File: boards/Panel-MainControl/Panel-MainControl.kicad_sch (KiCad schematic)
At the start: 16 parts, among them J1 ISP, J2 Raspberry_Pi_2_3, J3 BoardCon, J4 Panel, U1 ATmega48-20P, U2 ICL3232

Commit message: Initial schematics for panel control boards
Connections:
- net +3.3V: now also J2.1 (3V3), J2.17 (3V3)
- no-connect marks 13 -> 14
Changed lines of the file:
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@@
+	)
+	(no_connect
+		(at 146.05 74.93)
 	)
 	(no_connect
@@
 					(unit 1)
 				)
+			)
+		)
+	)
+	(symbol
+		(lib_id "power:+3.3V")
+		(at 156.21 74.93 0)
+		(unit 1)
+		(exclude_from_sim no)
+		(in_bom yes)
+		(on_board yes)
+		(dnp no)
+		(fields_autoplaced yes)
+		(property "Reference" "#PWR022"
+			(at 156.21 78.74 0)
+			(effects
+				(font
+					(size 1.27 1.27)
+				)
+				(hide yes)
+			)
+		)
+		(property "Value" "+3.3V"
+			(at 156.21 69.85 0)
+			(effects
+				(font
+					(size 1.27 1.27)
+				)
+			)
+		)
+		(property "Footprint" ""
+			(at 156.21 74.93 0)
+			(effects
+				(font
+					(size 1.27 1.27)
+				)
+				(hide yes)
+			)
+		)
+		(property "Datasheet" ""
+			(at 156.21 74.93 0)
+			(effects
+				(font
+					(size 1.27 1.27)
+				)
+				(hide yes)
+			)
+		)
+		(property "Description" "Power symbol creates a global label with name \"+3.3V\""
+			(at 156.21 74.93 0)
+			(effects
+				(font
+					(size 1.27 1.27)
+				)
+				(hide yes)
+			)
+		)
+		(pin "1"
+		)
+		(instances
+			(project "Panel-MainControl"
+				(path "/2777062a-260a-49c7-9a79-289c63518b5f"
+					(reference "#PWR022")
+					(unit 1)
+				)

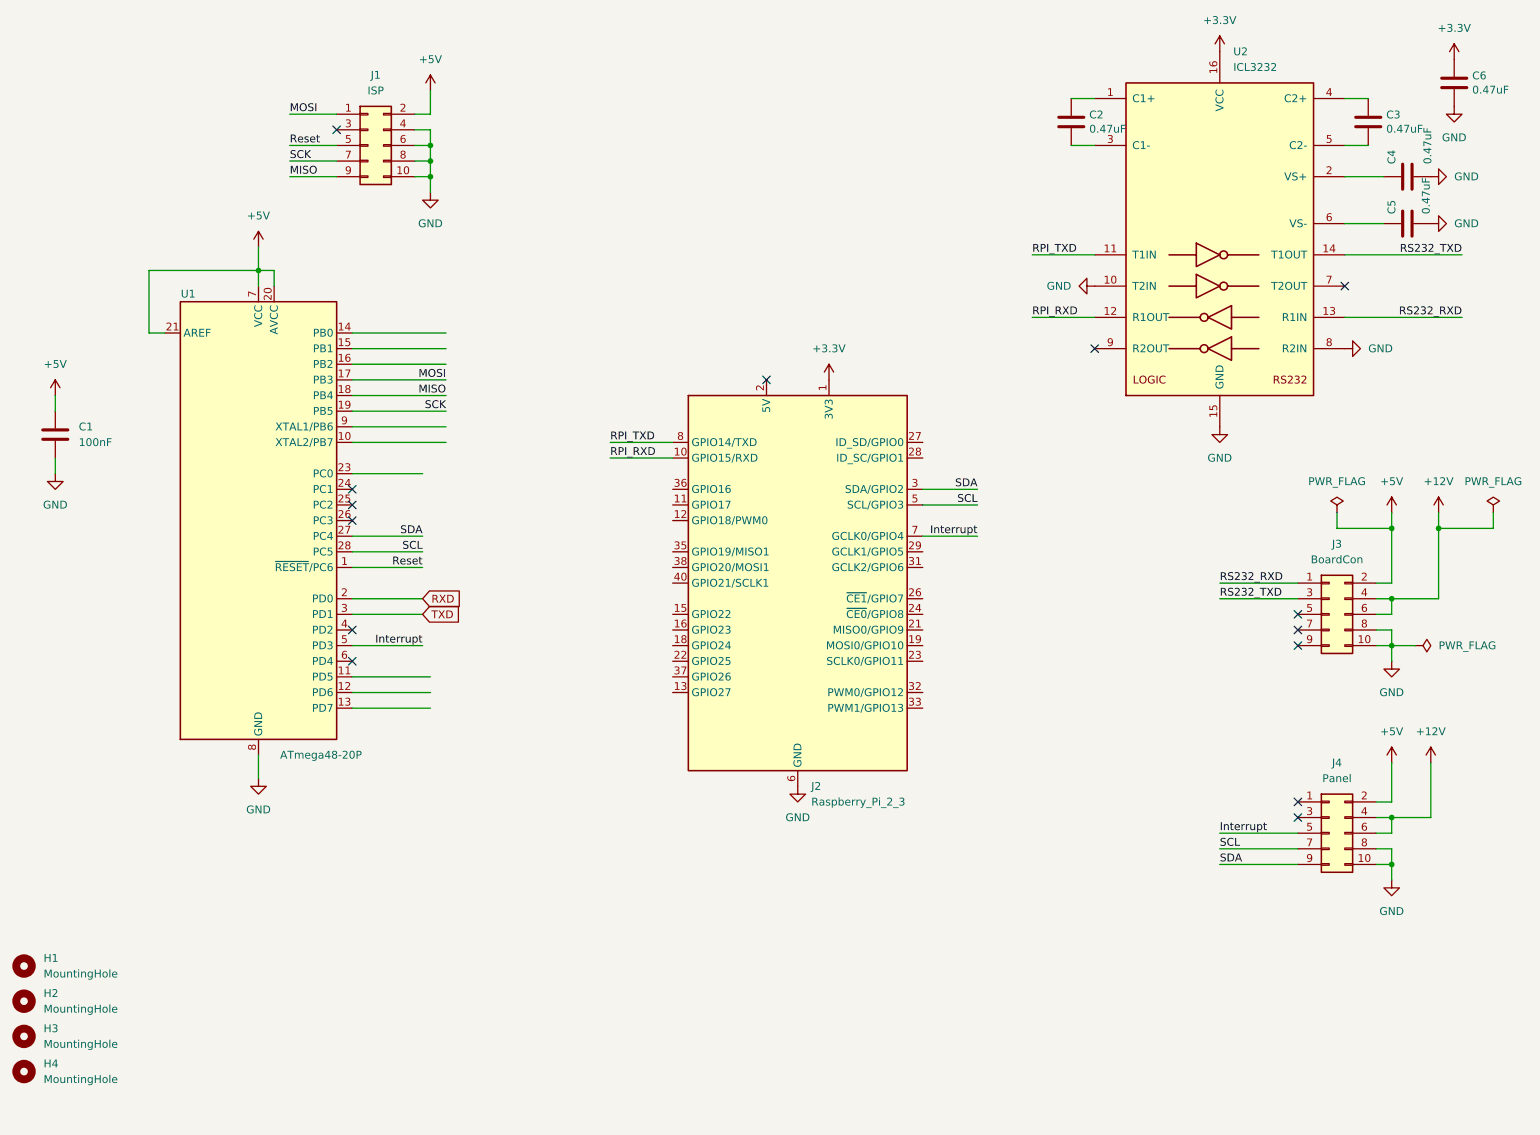
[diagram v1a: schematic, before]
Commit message: Added panel design files and panel schematics
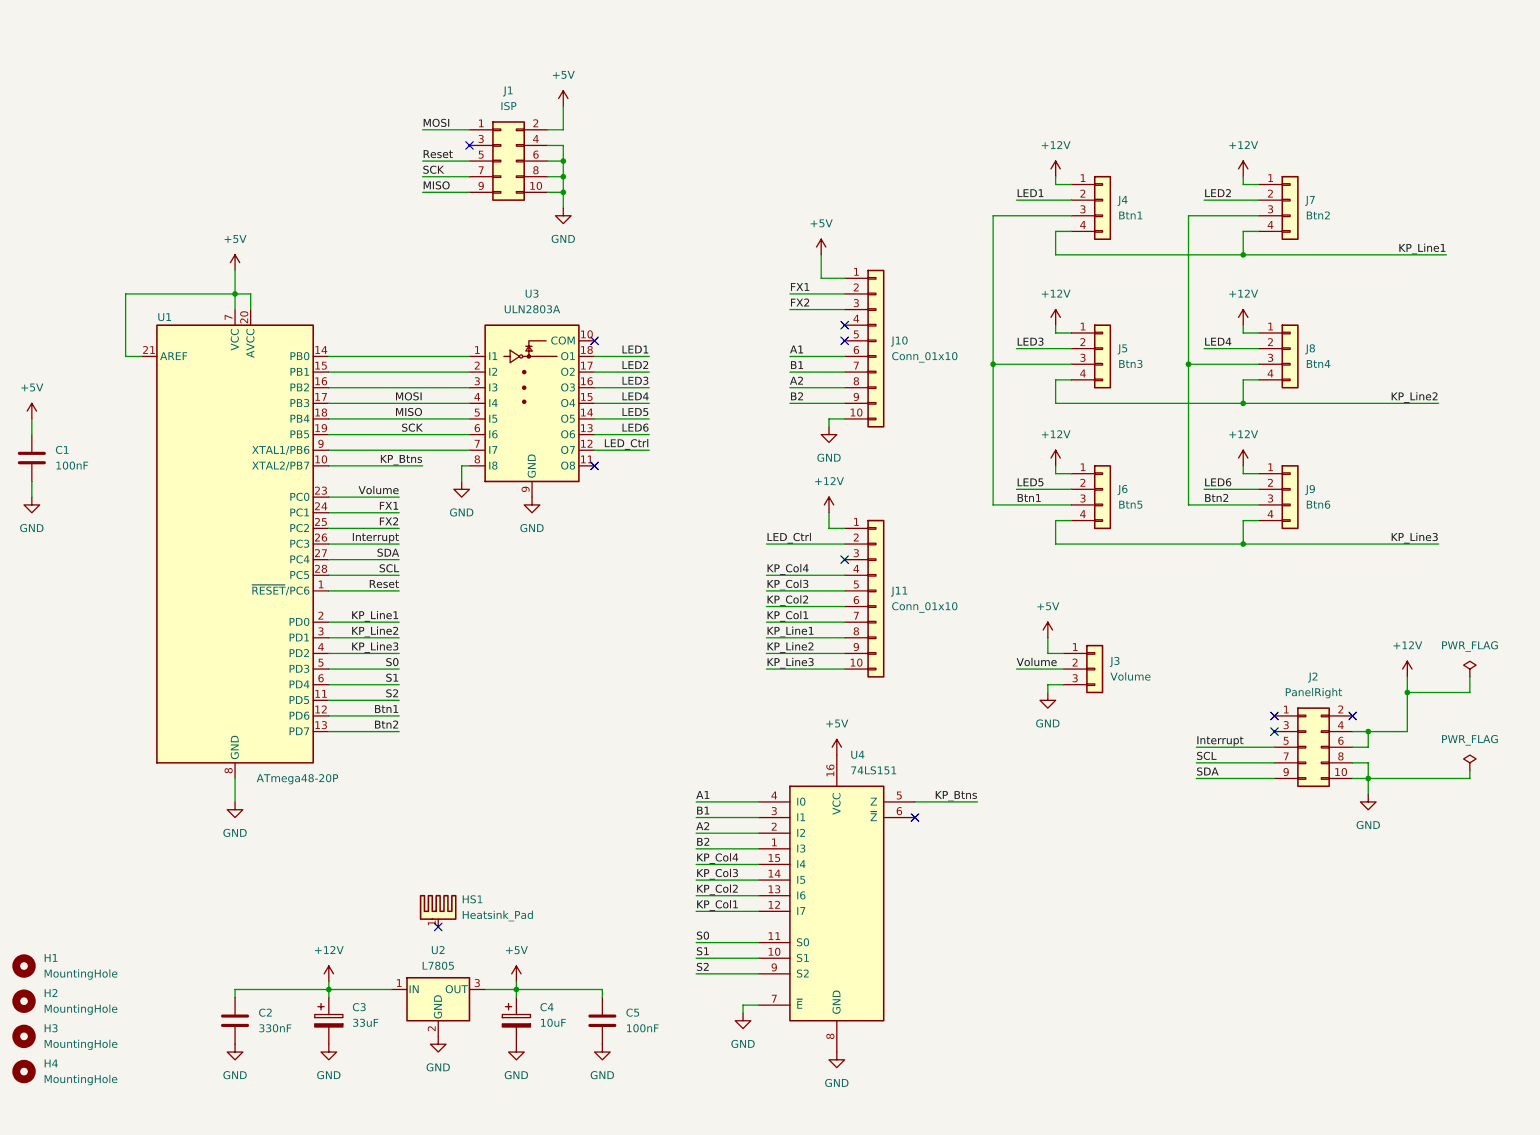
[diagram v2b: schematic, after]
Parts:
- removed C3, C4, C6: 0.47uF, Capacitor_THT:C_Rect_L7.0mm_W3.5mm_P5.00mm, symbol Device:C
- removed J2: Raspberry_Pi_2_3, Connector_PinHeader_2.54mm:PinHeader_2x20_P2.54mm_Vertical, symbol Connector:Raspberry_Pi_2_3
- removed J3: BoardCon, Connector_IDC:IDC-Header_2x05_P2.54mm_Vertical, symbol Connector_Generic:Conn_02x05_Odd_Even
- removed J4: Panel, Connector_IDC:IDC-Header_2x05_P2.54mm_Vertical, symbol Connector_Generic:Conn_02x05_Odd_Even
- removed U2: ICL3232, Package_DIP:DIP-16_W7.62mm, symbol Interface_UART:ICL3232
- added C3: 33uF, Capacitor_THT:CP_Radial_D7.5mm_P2.50mm, symbol Device:C_Polarized
- added C4: 10uF, Capacitor_THT:CP_Radial_D6.3mm_P2.50mm, symbol Device:C_Polarized
- added HS1: Heatsink_Pad, Custom_Heatsinks:Heatsink_Aavid_TO-220_H12.7mm, symbol Mechanical:Heatsink_Pad
- added J10, J11: Conn_01x10, Connector_PinHeader_1.27mm:PinHeader_1x10_P1.27mm_Vertical, symbol Connector_Generic:Conn_01x10
- added J2: PanelRight, Connector_IDC:IDC-Header_2x05_P2.54mm_Vertical, symbol Connector_Generic:Conn_02x05_Odd_Even
- added J3: Volume, Connector_PinHeader_2.54mm:PinHeader_1x03_P2.54mm_Vertical, symbol Connector_Generic:Conn_01x03
- added J4: Btn1, Connector_JST:JST_XH_B4B-XH-A_1x04_P2.50mm_Vertical, symbol Connector_Generic:Conn_01x04
- added J5: Btn3, Connector_JST:JST_XH_B4B-XH-A_1x04_P2.50mm_Vertical, symbol Connector_Generic:Conn_01x04
- added J6: Btn5, Connector_JST:JST_XH_B4B-XH-A_1x04_P2.50mm_Vertical, symbol Connector_Generic:Conn_01x04
- added J7: Btn2, Connector_JST:JST_XH_B4B-XH-A_1x04_P2.50mm_Vertical, symbol Connector_Generic:Conn_01x04
- added J8: Btn4, Connector_JST:JST_XH_B4B-XH-A_1x04_P2.50mm_Vertical, symbol Connector_Generic:Conn_01x04
- added J9: Btn6, Connector_JST:JST_XH_B4B-XH-A_1x04_P2.50mm_Vertical, symbol Connector_Generic:Conn_01x04
- added U2: L7805, Package_TO_SOT_THT:TO-220-3_Vertical, symbol Regulator_Linear:L7805
- added U3: ULN2803A, Package_DIP:DIP-18_W7.62mm, symbol Transistor_Array:ULN2803A
- added U4: 74LS151, Package_DIP:DIP-16_W7.62mm, symbol 74xx:74LS151
- C2: value 0.47uF -> 330nF; footprint Capacitor_THT:C_Rect_L7.0mm_W3.5mm_P5.00mm -> Capacitor_THT:C_Disc_D4.3mm_W1.9mm_P5.00mm; Supplier Digikey -> (none); Supplier_Ref 445-173138-1-ND -> (none); Type MLCC -> (none); Voltage 50V -> (none)
- C5: value 0.47uF -> 100nF; footprint Capacitor_THT:C_Rect_L7.0mm_W3.5mm_P5.00mm -> Capacitor_THT:C_Disc_D4.3mm_W1.9mm_P5.00mm; Supplier Digikey -> (none); Supplier_Ref 445-173138-1-ND -> (none); Type MLCC -> (none); Voltage 50V -> (none)
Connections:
- net +12V: now also C2.1, C3.1, J11.1 (Pin_1), J2.4 (Pin_4), J2.6 (Pin_6), J4.1 (Pin_1), J5.1 (Pin_1), J6.1 (Pin_1), J7.1 (Pin_1), J8.1 (Pin_1), J9.1 (Pin_1), U2.1 (IN)
- net +5V: now also C5.1, C4.1, J10.1 (Pin_1), J3.1 (Pin_1), U2.3 (OUT), U4.16 (VCC)
- net GND: now also C2.2, C3.2, C4.2, J10.10 (Pin_10), J2.10 (Pin_10), J2.8 (Pin_8), J3.3 (Pin_3), U2.2 (GND), U3.8 (I8), U3.9 (GND), U4.7 (~{E}), U4.8 (GND)
- net Interrupt: now also U1.26 (PC3), J2.5 (Pin_5); no longer U1.5 (PD3)
- net MISO: now also U3.5 (I5)
- net MOSI: now also U3.4 (I4)
- net SCK: now also U3.6 (I6)
- net SCL: now also J2.7 (Pin_7)
- net SDA: now also J2.9 (Pin_9)
- net KP_Btns: now reaches U1.10 (XTAL2/PB7)
- net KP_Btns: now also U4.5 (Z)
- net S2: now reaches U1.11 (PD5)
- net S2: now also U4.9 (S2)
- net Btn1: now reaches U1.12 (PD6)
- net Btn1: now also J4.3 (Pin_3), J5.3 (Pin_3), J6.3 (Pin_3)
- net Btn2: now reaches U1.13 (PD7)
- net Btn2: now also J7.3 (Pin_3), J8.3 (Pin_3), J9.3 (Pin_3)
- net at U1.14 (PB0): now also U3.1 (I1)
- net at U1.15 (PB1): now also U3.2 (I2)
- net at U1.16 (PB2): now also U3.3 (I3)
- net Volume: now reaches U1.23 (PC0)
- net Volume: now also J3.2 (Pin_2)
- net FX1: now reaches U1.24 (PC1)
- net FX1: now also J10.2 (Pin_2)
- net FX2: now reaches U1.25 (PC2)
- net FX2: now also J10.3 (Pin_3)
- net KP_Line3: now reaches U1.4 (PD2)
- net KP_Line3: now also J11.10 (Pin_10), J6.4 (Pin_4), J9.4 (Pin_4)
- net S1: now reaches U1.6 (PD4)
- net S1: now also U4.10 (S1)
- net at U1.9 (XTAL1/PB6): now also U3.7 (I7)
- net RXD renamed KP_Line1
- net KP_Line1: now also J11.8 (Pin_8), J4.4 (Pin_4), J7.4 (Pin_4)
- net TXD renamed KP_Line2
- net KP_Line2: now also J11.9 (Pin_9), J5.4 (Pin_4), J8.4 (Pin_4)
- new net A1: J10.6 (Pin_6), U4.4 (I0)
- new net A2: J10.8 (Pin_8), U4.2 (I2)
- new net B1: J10.7 (Pin_7), U4.3 (I1)
- new net B2: J10.9 (Pin_9), U4.1 (I3)
- new net KP_Col1: J11.7 (Pin_7), U4.12 (I7)
- new net KP_Col2: J11.6 (Pin_6), U4.13 (I6)
- new net KP_Col3: J11.5 (Pin_5), U4.14 (I5)
- new net KP_Col4: J11.4 (Pin_4), U4.15 (I4)
- new net LED1: J4.2 (Pin_2), U3.18 (O1)
- new net LED2: J7.2 (Pin_2), U3.17 (O2)
- new net LED3: J5.2 (Pin_2), U3.16 (O3)
- new net LED4: J8.2 (Pin_2), U3.15 (O4)
- new net LED5: J6.2 (Pin_2), U3.14 (O5)
- new net LED6: J9.2 (Pin_2), U3.13 (O6)
- new net LED_Ctrl: J11.2 (Pin_2), U3.12 (O7)
- new net S0: U1.5 (PD3), U4.11 (S0)
- no-connect marks 14 -> 11

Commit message: Finished PCB layouts for panel keypad
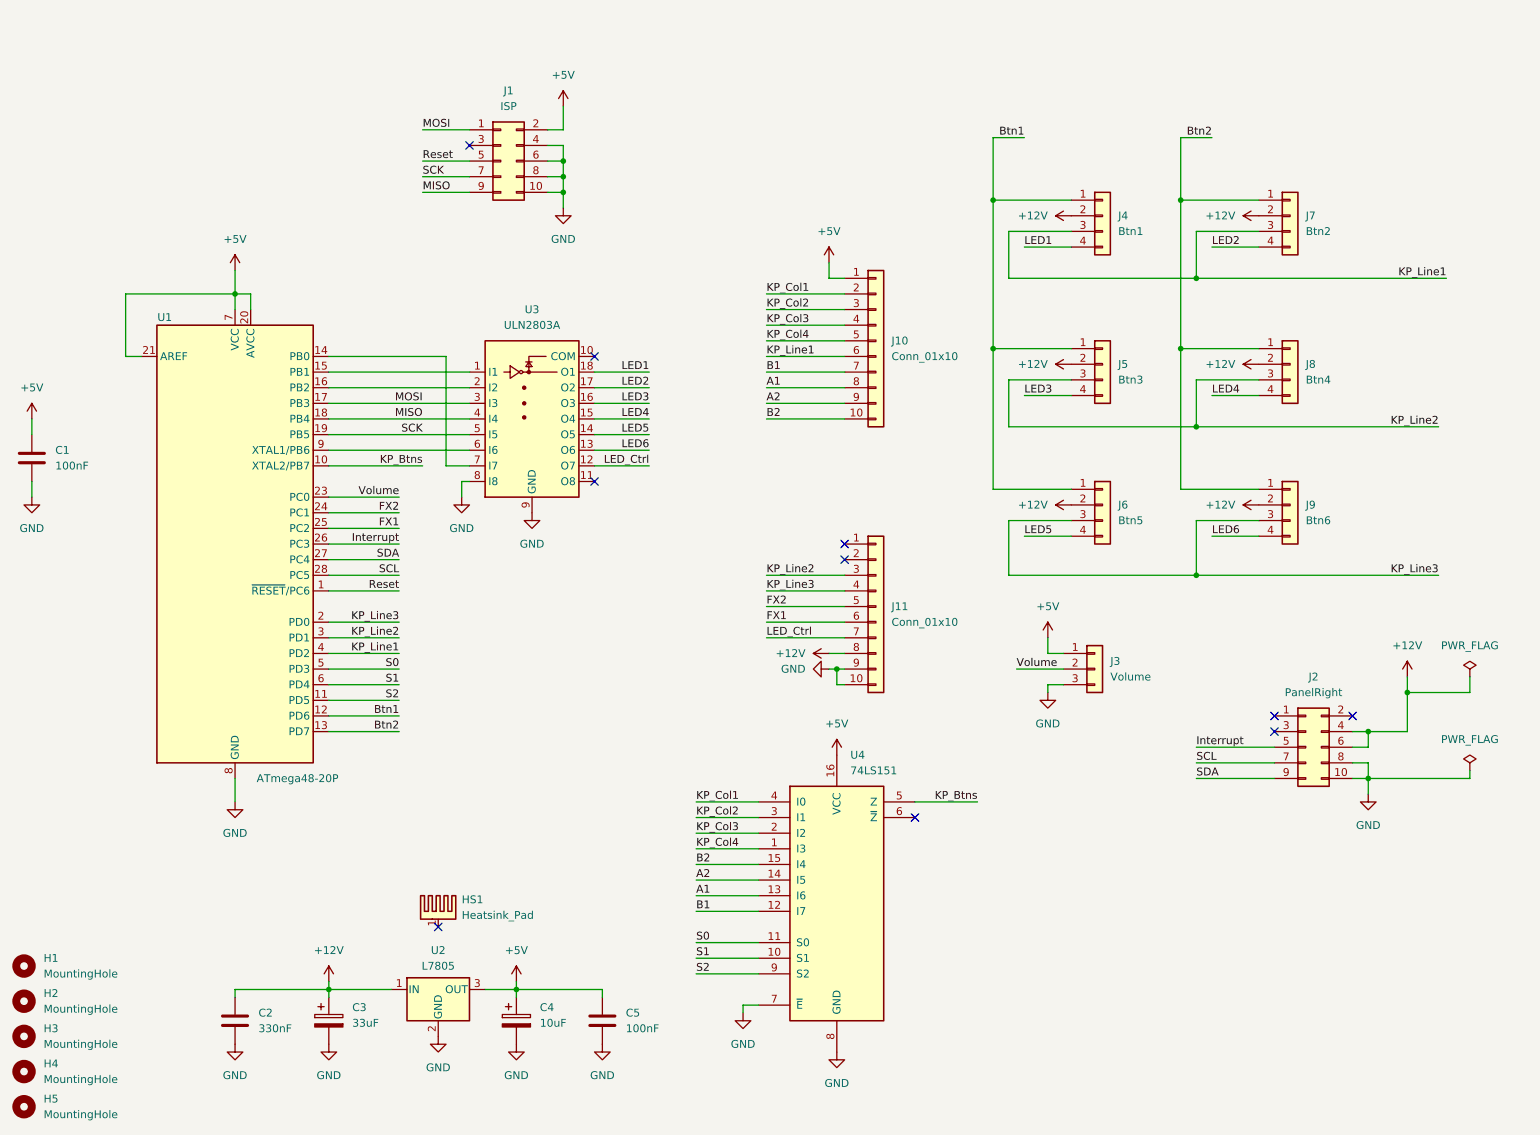
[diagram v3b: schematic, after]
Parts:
- added H5: MountingHole, MountingHole:MountingHole_2.7mm_M2.5, symbol Mechanical:MountingHole
- H1, H2, H3, H4: footprint MountingHole:MountingHole_3mm -> MountingHole:MountingHole_2.7mm_M2.5
- J10, J11: footprint Connector_PinHeader_1.27mm:PinHeader_1x10_P1.27mm_Vertical -> Connector_PinHeader_2.00mm:PinHeader_1x10_P2.00mm_Vertical
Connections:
- net +12V: now also J11.8 (Pin_8), J4.2 (Pin_2), J5.2 (Pin_2), J6.2 (Pin_2), J7.2 (Pin_2), J8.2 (Pin_2), J9.2 (Pin_2); no longer J11.1 (Pin_1), J4.1 (Pin_1), J5.1 (Pin_1), J6.1 (Pin_1), J7.1 (Pin_1), J8.1 (Pin_1), J9.1 (Pin_1)
- net A1: now also J10.8 (Pin_8), U4.13 (I6); no longer J10.6 (Pin_6), U4.4 (I0)
- net A2: now also J10.9 (Pin_9), U4.14 (I5); no longer J10.8 (Pin_8), U4.2 (I2)
- net B1: now also U4.12 (I7); no longer U4.3 (I1)
- net B2: now also J10.10 (Pin_10), U4.15 (I4); no longer J10.9 (Pin_9), U4.1 (I3)
- net Btn1: now also J4.1 (Pin_1), J5.1 (Pin_1), J6.1 (Pin_1); no longer J4.3 (Pin_3), J5.3 (Pin_3), J6.3 (Pin_3)
- net Btn2: now also J7.1 (Pin_1), J8.1 (Pin_1), J9.1 (Pin_1); no longer J7.3 (Pin_3), J8.3 (Pin_3), J9.3 (Pin_3)
- net FX1: now also J11.6 (Pin_6), U1.25 (PC2); no longer J10.2 (Pin_2), U1.24 (PC1)
- net FX2: now also J11.5 (Pin_5), U1.24 (PC1); no longer J10.3 (Pin_3), U1.25 (PC2)
- net GND: now also J11.10 (Pin_10), J11.9 (Pin_9); no longer J10.10 (Pin_10)
- net KP_Col1: now also J10.2 (Pin_2), U4.4 (I0); no longer J11.7 (Pin_7), U4.12 (I7)
- net KP_Col2: now also J10.3 (Pin_3), U4.3 (I1); no longer J11.6 (Pin_6), U4.13 (I6)
- net KP_Col3: now also J10.4 (Pin_4), U4.2 (I2); no longer J11.5 (Pin_5), U4.14 (I5)
- net KP_Col4: now also J10.5 (Pin_5), U4.1 (I3); no longer J11.4 (Pin_4), U4.15 (I4)
- net KP_Line1: now also J10.6 (Pin_6), J4.3 (Pin_3), J7.3 (Pin_3), U1.4 (PD2); no longer J11.8 (Pin_8), J4.4 (Pin_4), J7.4 (Pin_4), U1.2 (PD0)
- net KP_Line2: now also J11.3 (Pin_3), J5.3 (Pin_3), J8.3 (Pin_3); no longer J11.9 (Pin_9), J5.4 (Pin_4), J8.4 (Pin_4)
- net KP_Line3: now also J11.4 (Pin_4), J6.3 (Pin_3), J9.3 (Pin_3), U1.2 (PD0); no longer J11.10 (Pin_10), J6.4 (Pin_4), J9.4 (Pin_4), U1.4 (PD2)
- net LED1: now also J4.4 (Pin_4); no longer J4.2 (Pin_2)
- net LED2: now also J7.4 (Pin_4); no longer J7.2 (Pin_2)
- net LED3: now also J5.4 (Pin_4); no longer J5.2 (Pin_2)
- net LED4: now also J8.4 (Pin_4); no longer J8.2 (Pin_2)
- net LED5: now also J6.4 (Pin_4); no longer J6.2 (Pin_2)
- net LED6: now also J9.4 (Pin_4); no longer J9.2 (Pin_2)
- net LED_Ctrl: now also J11.7 (Pin_7); no longer J11.2 (Pin_2)
- net MISO: now also U3.4 (I4); no longer U3.5 (I5)
- net MOSI: now also U3.3 (I3); no longer U3.4 (I4)
- net SCK: now also U3.5 (I5); no longer U3.6 (I6)
- net at U1.14 (PB0): now also U3.7 (I7); no longer U3.1 (I1)
- net at U1.15 (PB1): now also U3.1 (I1); no longer U3.2 (I2)
- net at U1.16 (PB2): now also U3.2 (I2); no longer U3.3 (I3)
- net at U1.9 (XTAL1/PB6): now also U3.6 (I6); no longer U3.7 (I7)
- no-connect marks 11 -> 10
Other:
- moved on the sheet: J11, J4, J5, J6, J7, J8, J9, U3
